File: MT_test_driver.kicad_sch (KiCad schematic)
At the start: 43 parts, among them J2 USB_B_Micro, J4 Barrel_Jack, SW1 SW_SPDT, SW2 SW_SPDT, U1 INA219AxD, U2 STM32F405RGTx, U3 DRV8871DDA, U4 USBLC6-2SC6, U5 AMS1117-3.3, Y2 16MHz

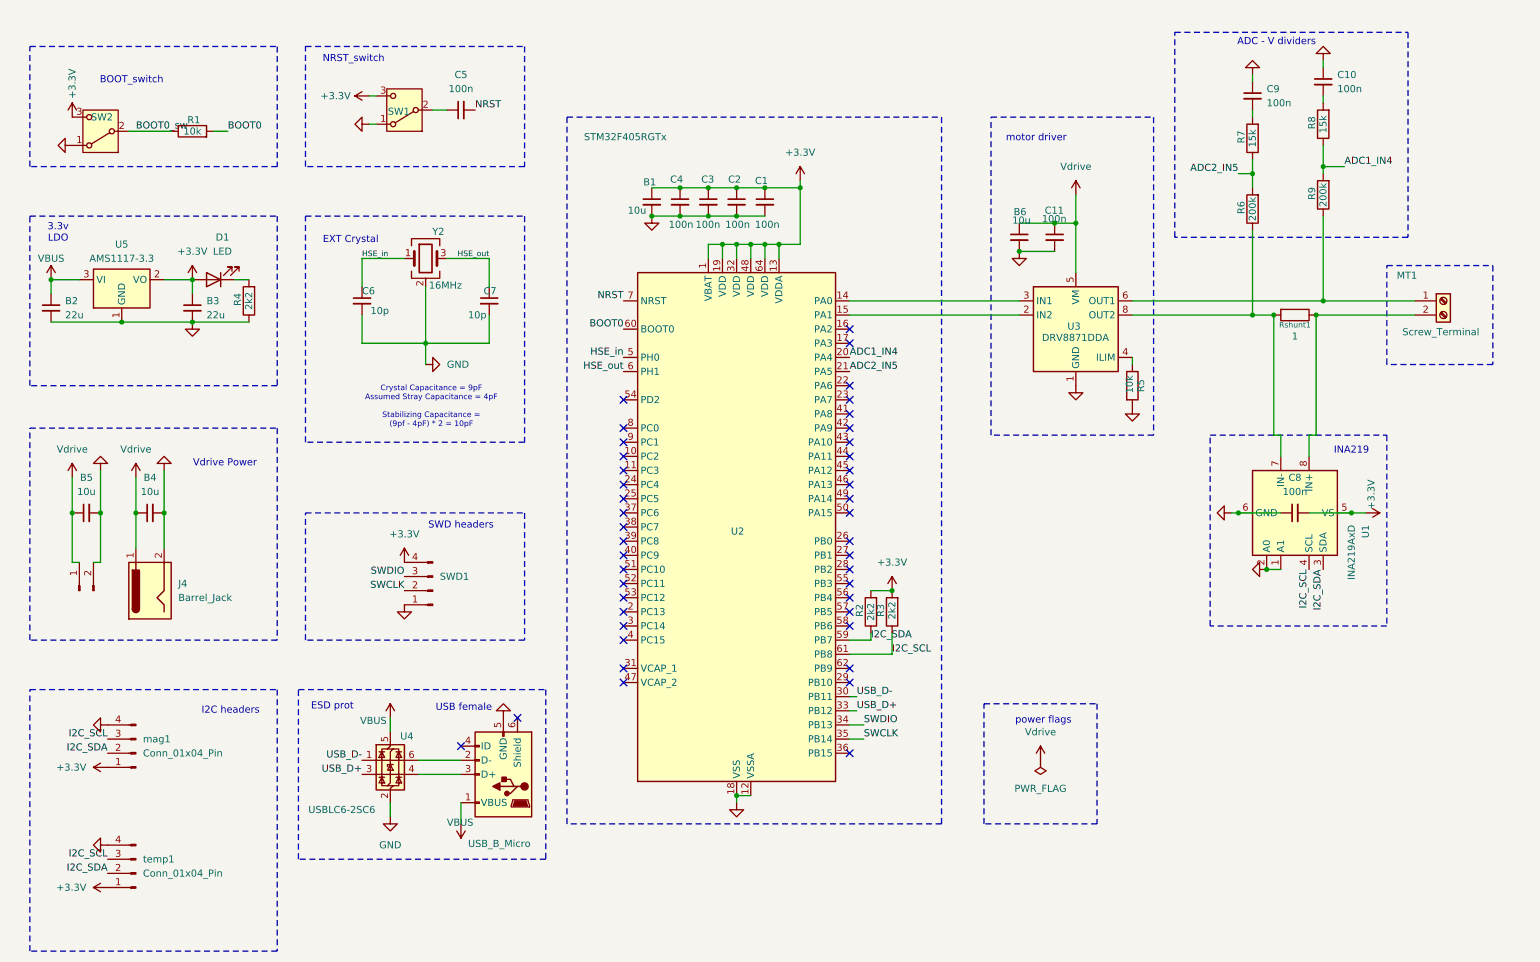
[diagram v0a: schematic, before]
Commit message: updated schematic to look more professional, changeda few components like micro usb type b to type c etc
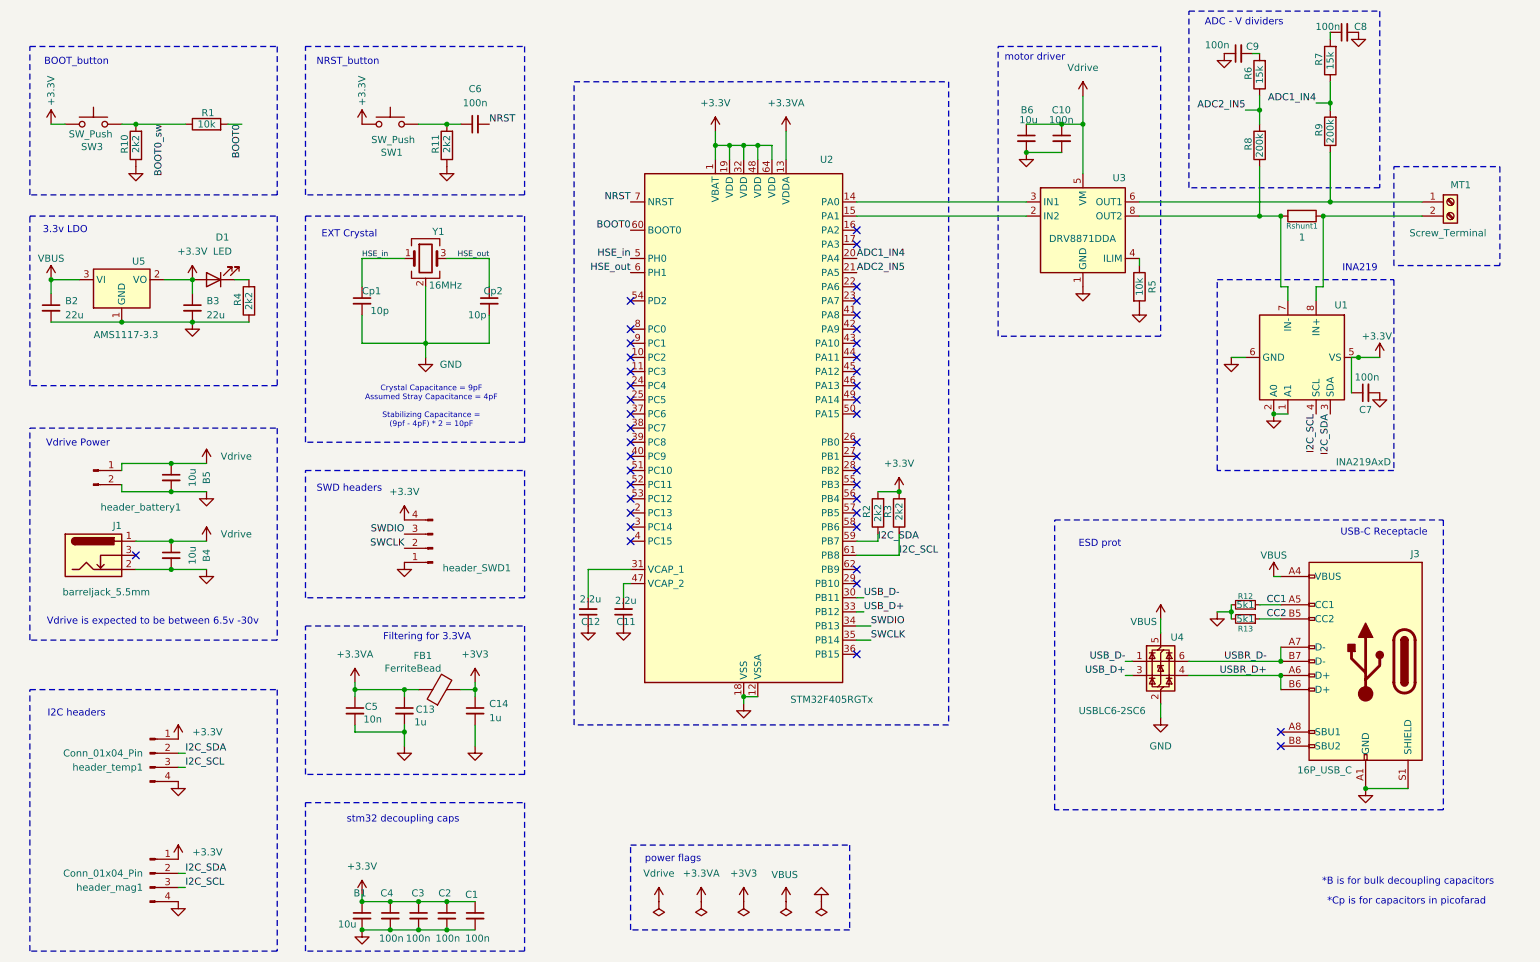
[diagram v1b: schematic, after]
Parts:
- removed J2: USB_B_Micro, symbol Connector:USB_B_Micro
- removed J4: Barrel_Jack, symbol Connector:Barrel_Jack
- removed SW1, SW2: SW_SPDT, symbol Switch:SW_SPDT
- added C11, C12: 2.2u, Capacitor_SMD:C_0805_2012Metric_Pad1.18x1.45mm_HandSolder, symbol Device:C_Small
- added C13, C14: 1u, Capacitor_SMD:C_0805_2012Metric_Pad1.18x1.45mm_HandSolder, symbol Device:C_Small
- added C5: 10n, Capacitor_SMD:C_0805_2012Metric_Pad1.18x1.45mm_HandSolder, symbol Device:C_Small
- added FB1: FerriteBead, Inductor_SMD:L_0805_2012Metric_Pad1.05x1.20mm_HandSolder, symbol Device:FerriteBead
- added J1: barreljack_5.5mm, Connector_BarrelJack:BarrelJack_Horizontal, symbol Connector:Barrel_Jack_Switch
- added J3: 16P_USB_C, Connector_USB:USB_C_Receptacle_G-Switch_GT-USB-7010ASV, symbol Connector:USB_C_Receptacle_USB2.0_16P
- added R10, R11: 2k2, Resistor_SMD:R_0805_2012Metric_Pad1.20x1.40mm_HandSolder, symbol Device:R
- added R12, R13: 5k1, Resistor_SMD:R_0805_2012Metric_Pad1.20x1.40mm_HandSolder, symbol Device:R_Small
- added SW1, SW3: SW_Push, Library:tactile switch 4.5_4.5, symbol Switch:SW_Push
- B1, B2, B3, B4, B5, B6, C1, C2, C3, C4, C9: footprint (none) -> Capacitor_SMD:C_0805_2012Metric_Pad1.18x1.45mm_HandSolder
- C10: renamed from C11; footprint (none) -> Capacitor_SMD:C_0805_2012Metric_Pad1.18x1.45mm_HandSolder
- C6: renamed from C5; footprint (none) -> Capacitor_SMD:C_0805_2012Metric_Pad1.18x1.45mm_HandSolder
- C7: renamed from C8; footprint (none) -> Capacitor_SMD:C_0805_2012Metric_Pad1.18x1.45mm_HandSolder
- C8: renamed from C10; footprint (none) -> Capacitor_SMD:C_0805_2012Metric_Pad1.18x1.45mm_HandSolder
- D1: footprint (none) -> LED_SMD:LED_0805_2012Metric_Pad1.15x1.40mm_HandSolder
- MT1: footprint (none) -> TerminalBlock_Phoenix:TerminalBlock_Phoenix_MPT-0,5-2-2.54_1x02_P2.54mm_Horizontal
- R1, R2, R3, R4, R5: footprint (none) -> Resistor_SMD:R_0805_2012Metric_Pad1.20x1.40mm_HandSolder
- R6: renamed from R7; footprint (none) -> Resistor_SMD:R_0603_1608Metric_Pad0.98x0.95mm_HandSolder
- R7: renamed from R8; footprint (none) -> Resistor_SMD:R_0603_1608Metric_Pad0.98x0.95mm_HandSolder
- R8: renamed from R6; footprint (none) -> Resistor_SMD:R_0603_1608Metric_Pad0.98x0.95mm_HandSolder
- R9: footprint (none) -> Resistor_SMD:R_0603_1608Metric_Pad0.98x0.95mm_HandSolder
- Rshunt1: footprint (none) -> Resistor_SMD:R_2512_6332Metric_Pad1.40x3.35mm_HandSolder
- header_SWD1: renamed from SWD1; footprint (none) -> Connector_PinHeader_2.54mm:PinHeader_1x04_P2.54mm_Vertical
- header_battery1: renamed from battery_header1; footprint (none) -> Connector_PinHeader_2.54mm:PinHeader_1x02_P2.54mm_Vertical
- header_mag1: renamed from mag1; footprint (none) -> Connector_PinHeader_2.54mm:PinHeader_1x04_P2.54mm_Vertical
- header_temp1: renamed from temp1; footprint (none) -> Connector_PinHeader_2.54mm:PinHeader_1x04_P2.54mm_Vertical
- renumbered C6 to Cp1, C7 to Cp2, Y2 to Y1
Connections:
- net +3.3V: now also C7.1, SW1.1, SW3.1; no longer C7.2, U2.13 (VDDA)
- net BOOT0_sw: now also R10.2, SW3.2
- net GND: now also C7.2, C8.2, C11.1, C12.1, C13.2, C14.2, C5.2, J1.2, J3.A1 (GND), J3.A12 (GND), J3.B1 (GND), J3.B12 (GND), J3.S1 (SHIELD), R10.1, R11.1, R12.2, R13.2; no longer C7.1, C8.1
- net VBUS: now also J3.A4 (VBUS), J3.A9 (VBUS), J3.B4 (VBUS), J3.B9 (VBUS)
- net Vdrive: now also J1.1
- net USBR_D-: now reaches U4.6 (I/O1)
- net USBR_D-: now also J3.A7 (D-), J3.B7 (D-)
- net USBR_D+: now reaches U4.4 (I/O2)
- net USBR_D+: now also J3.A6 (D+), J3.B6 (D+)
- net at U2.31 (VCAP_1): now also C12.2
- net at U2.47 (VCAP_2): now also C11.2
- net at C6.1: now also R11.2, SW1.2
- net at R7.2: now also C8.1; no longer C8.2
- new net +3.3VA: C13.1, C5.1, FB1.1, U2.13 (VDDA)
- new net +3V3: C14.1, FB1.2
- new net CC1: J3.A5 (CC1), R12.1
- new net CC2: J3.B5 (CC2), R13.1
- no-connect marks 43 -> 42
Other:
- note added: "*B is for bulk decoupling capacitors"
- note added: "*Cp is for capacitors in picofarad"
- note added: "BOOT_button"
- note added: "Filtering for 3.3VA"
- note added: "NRST_button"
- note added: "USB-C Receptacle"
- note added: "Vdrive is expected to be between 6.5v -30v"
- note added: "stm32 decoupling caps"
- note removed: "BOOT_switch"
- note removed: "NRST_switch"
- note removed: "USB female"
- moved on the sheet: B1, B4, B5, B6, C1, C10, C2, C3, C4, C6, C7, C8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

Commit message: assigned netclasses, constraints for PCB, small corrections
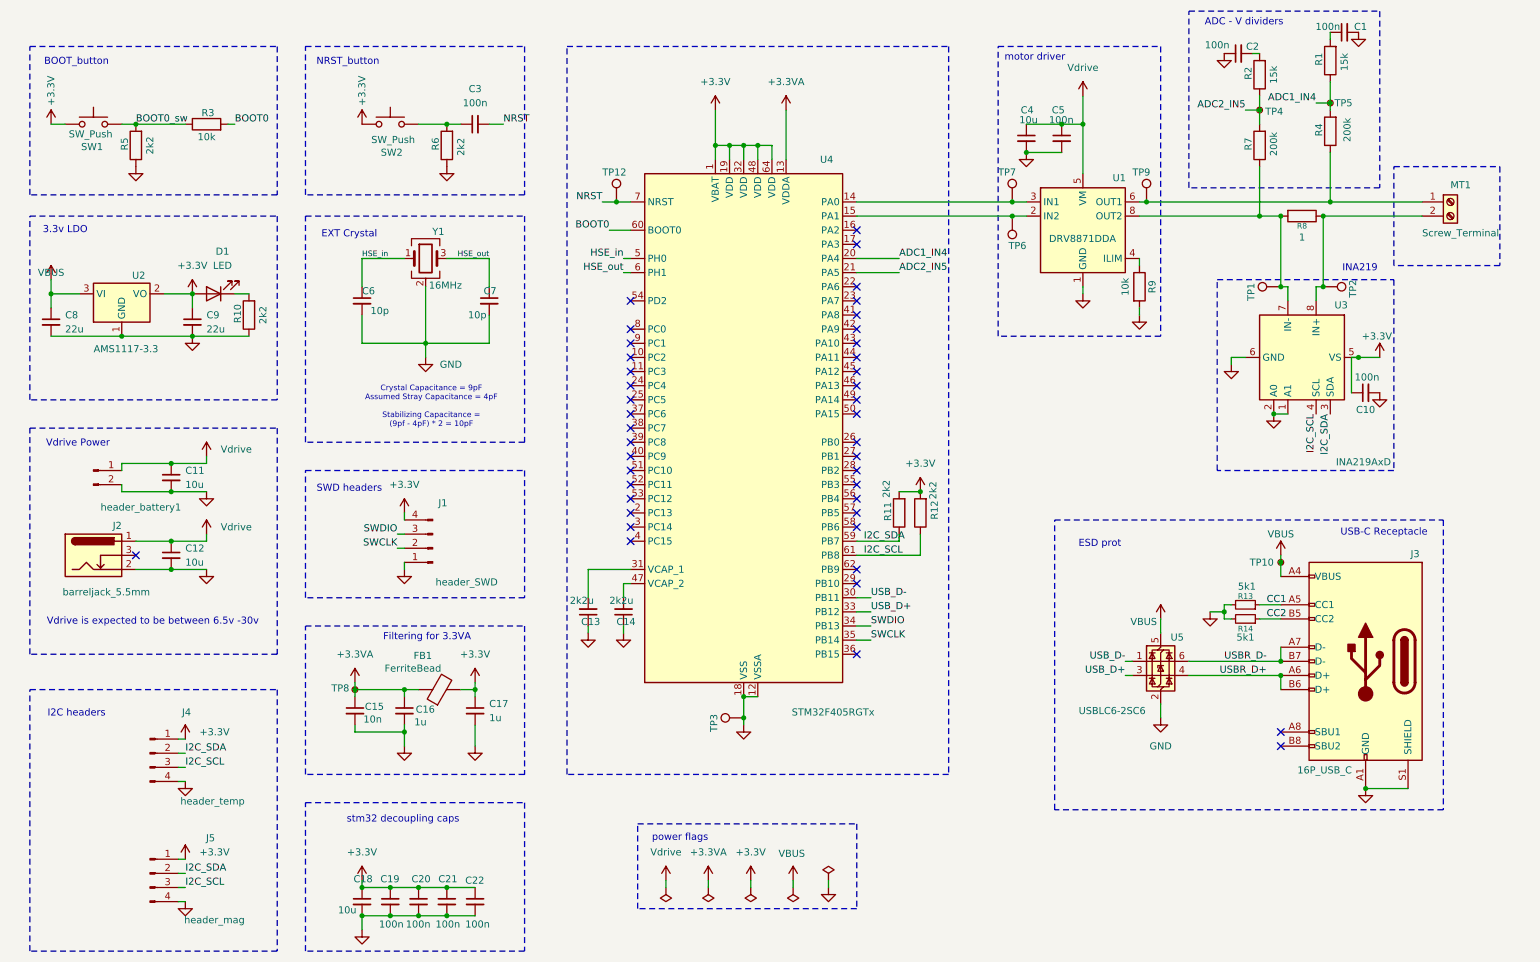
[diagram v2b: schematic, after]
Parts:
- added TP1, TP2, TP3, TP6, TP7, TP9: TestPoint, Connector_PinHeader_2.54mm:PinHeader_1x01_P2.54mm_Vertical, symbol Connector:TestPoint
- added TP10, TP4, TP5, TP8: TestPoint_Small, TestPoint:TestPoint_Pad_D1.5mm, symbol Connector:TestPoint_Small
- added TP12: TestPoint, TestPoint:TestPoint_Pad_D1.5mm, symbol Connector:TestPoint
- C13: renamed from C12; value 2.2u -> 2k2u
- C14: renamed from C11; value 2.2u -> 2k2u
- J1: renamed from header_SWD1; value Conn_01x04_Pin -> header_SWD
- J4: renamed from header_temp1; value Conn_01x04_Pin -> header_temp
- J5: renamed from header_mag1; value Conn_01x04_Pin -> header_mag
- renumbered C8 to C1, C7 to C10, B5 to C11, B4 to C12, C5 to C15, C13 to C16, C14 to C17, B1 to C18, C4 to C19, C9 to C2, C3 to C20, C2 to C21, C1 to C22, C6 to C3, B6 to C4, C10 to C5, Cp1 to C6, Cp2 to C7, B2 to C8, B3 to C9, J1 to J2, R7 to R1, R4 to R10, R2 to R11, R3 to R12, R12 to R13, R13 to R14, R6 to R2, R1 to R3, R9 to R4, R10 to R5, R11 to R6, R8 to R7, Rshunt1 to R8, R5 to R9, SW3 to SW1, SW1 to SW2, U3 to U1, U5 to U2, U1 to U3, U2 to U4, U4 to U5
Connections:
- net +3V3 is gone; now on net +3.3V: C17.1, FB1.2
- net +3.3VA: now also TP8.1
- net ADC1_IN4: now also TP5.1
- net ADC2_IN5: now also TP4.1
- net GND: now also TP3.1
- net NRST: now also TP12.1
- net VBUS: now also TP10.1
- net at MT1.1 (Pin_1), R4.1, U1.6 (OUT1): now also TP9.1
- net at U1.2 (IN2), U4.15 (PA1): now also TP6.1
- net at U1.3 (IN1), U4.14 (PA0): now also TP7.1
- net at R7.1, R8.2, U1.8 (OUT2)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: now also TP1.1
- net at MT1.2 (Pin_2), R8.1, U3.8 (IN+): now also TP2.1
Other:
- note removed: "*B is for bulk decoupling capacitors"
- note removed: "*Cp is for capacitors in picofarad"
- moved on the sheet: C18, C19, C20, C21, C22, C8, C9, D1, R10, R11, R12, U2
